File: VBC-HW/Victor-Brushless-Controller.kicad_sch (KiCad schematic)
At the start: 25 parts, among them Q1 TPH4R008NH, Q2 TPH4R008NH, Q3 TPH4R008NH, Q4 TPH4R008NH, Q5 TPH4R008NH, Q6 TPH4R008NH, U1 DRV8305NQPHPRQ1

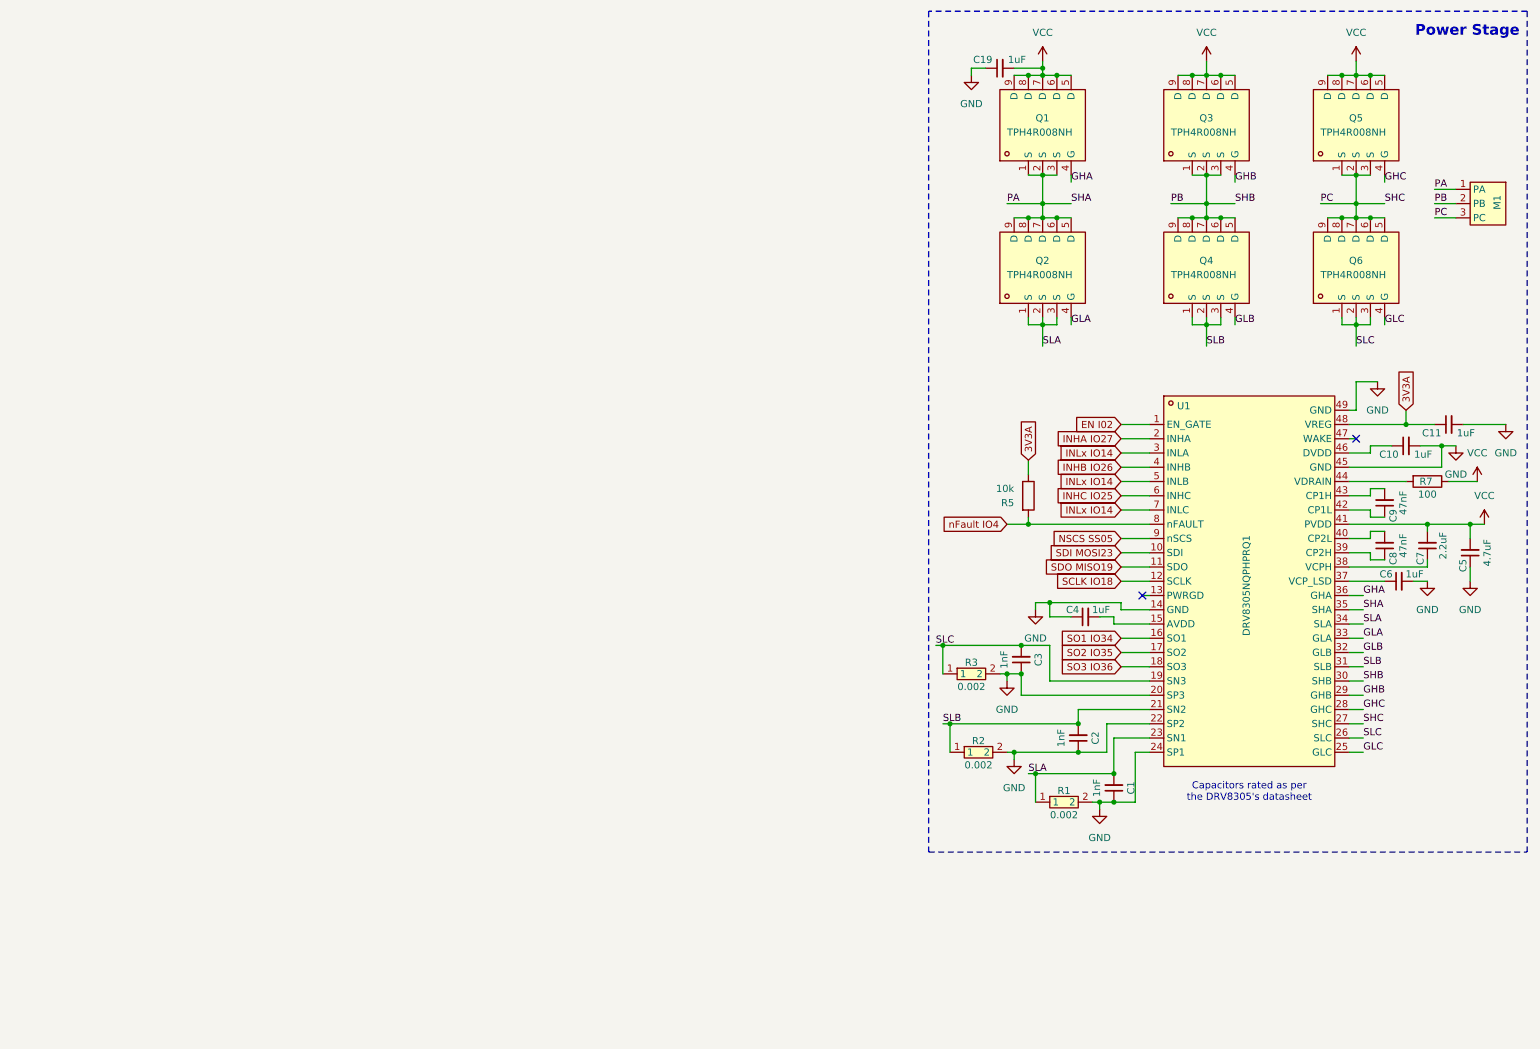
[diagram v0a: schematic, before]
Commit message: Added Kicad schematic magnetic, bus and temp
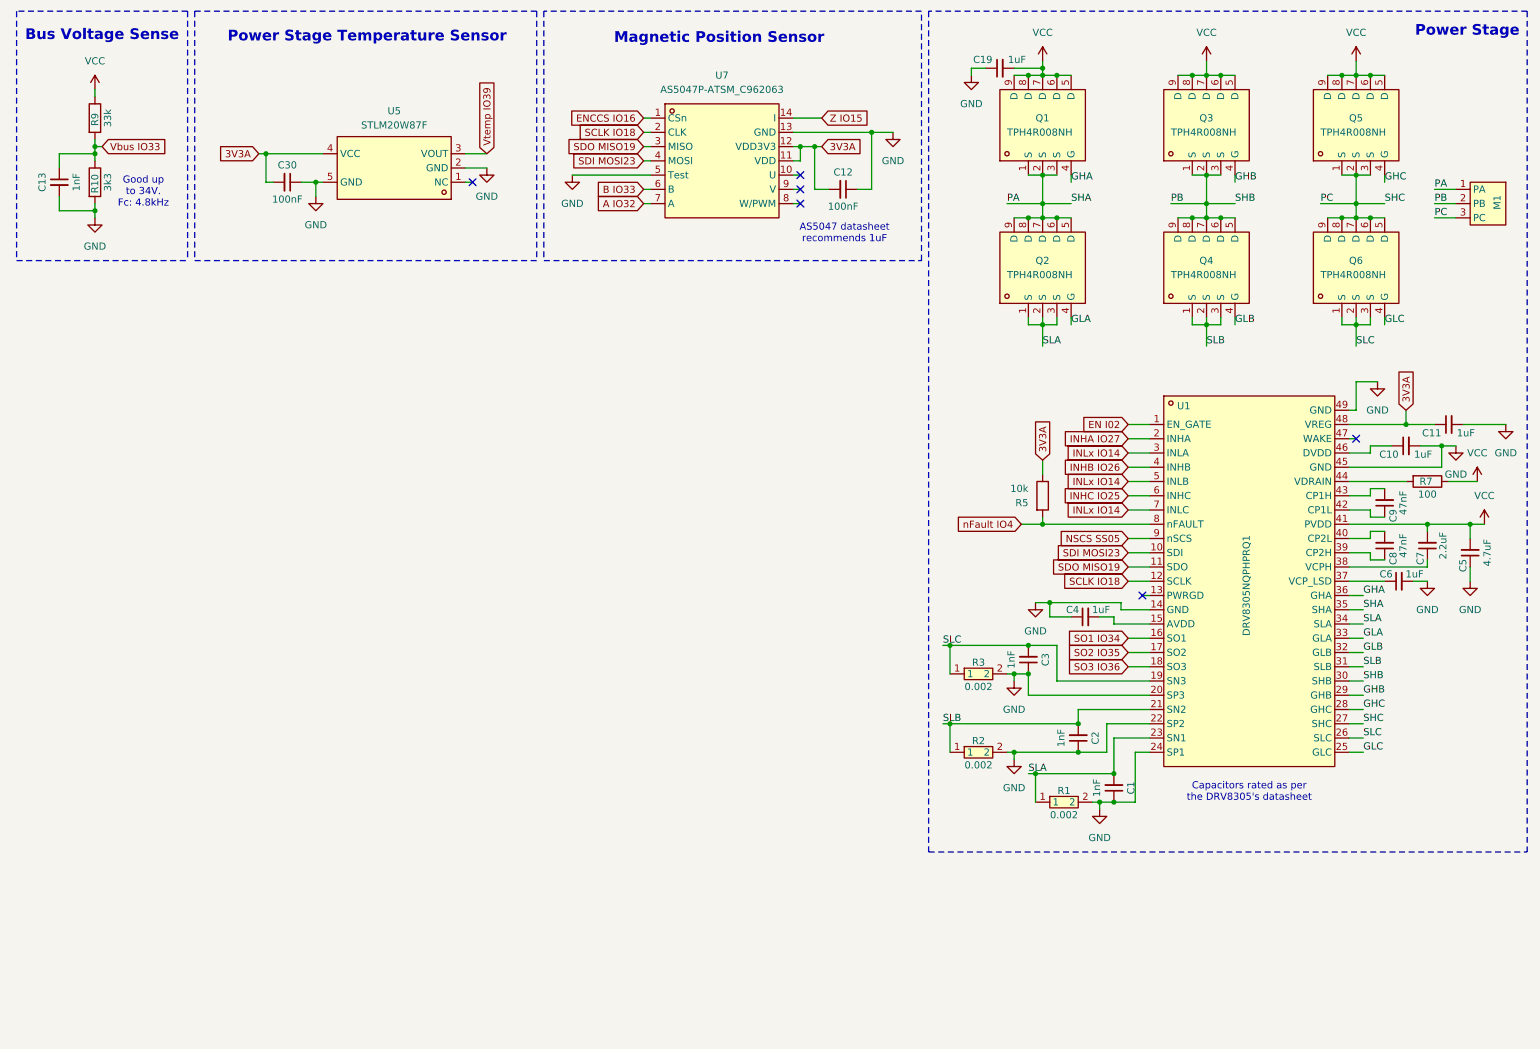
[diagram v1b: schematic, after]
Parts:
- added C12, C30: 100nF, symbol Device:C_Small
- added C13: 1nF, symbol Device:C_Small
- added R10: 3k3, symbol Device:R
- added R9: 33k, symbol Device:R
- added U5: STLM20W87F, easyeda2kicad:SOT-323-5_L2.1-W1.3-P0.65-LS2.1-BL, symbol STLM20W87F:STLM20W87F
- added U7: AS5047P-ATSM_C962063, easyeda2kicad:TSSOP-14_L5.0-W4.4-P0.65-LS6.4-BL, symbol AS5047P-ATSM:AS5047P-ATSM_C962063
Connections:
- net 3V3A: now also C12.2, C30.2, U5.4 (VCC), U7.11 (VDD), U7.12 (VDD3V3)
- net GND: now also C12.1, C13.2, C30.1, R10.2, U5.2 (GND), U5.5 (GND), U7.13 (GND), U7.5 (Test)
- net SCLK IO18: now also U7.2 (CLK)
- net SDI MOSI23: now also U7.4 (MOSI)
- net SDO MISO19: now also U7.3 (MISO)
- net VCC: now also R9.1
- new net A IO32: U7.7 (A)
- new net B IO33: U7.6 (B)
- new net ENCCS IO16: U7.1 (CSn)
- new net Vbus IO33: C13.1, R10.1, R9.2
- new net Vtemp IO39: U5.3 (VOUT)
- new net Z IO15: U7.14 (I)
- no-connect marks 2 -> 6
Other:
- note added: "AS5047 datasheet recommends 1uF"
- note added: "Bus Voltage Sense"
- note added: "Good up to 34V. Fc: 4.8kHz"
- note added: "Magnetic Position Sensor"
- note added: "Power Stage Temperature Sensor"
- moved on the sheet: C3, R3, R5

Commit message: Added buck converter
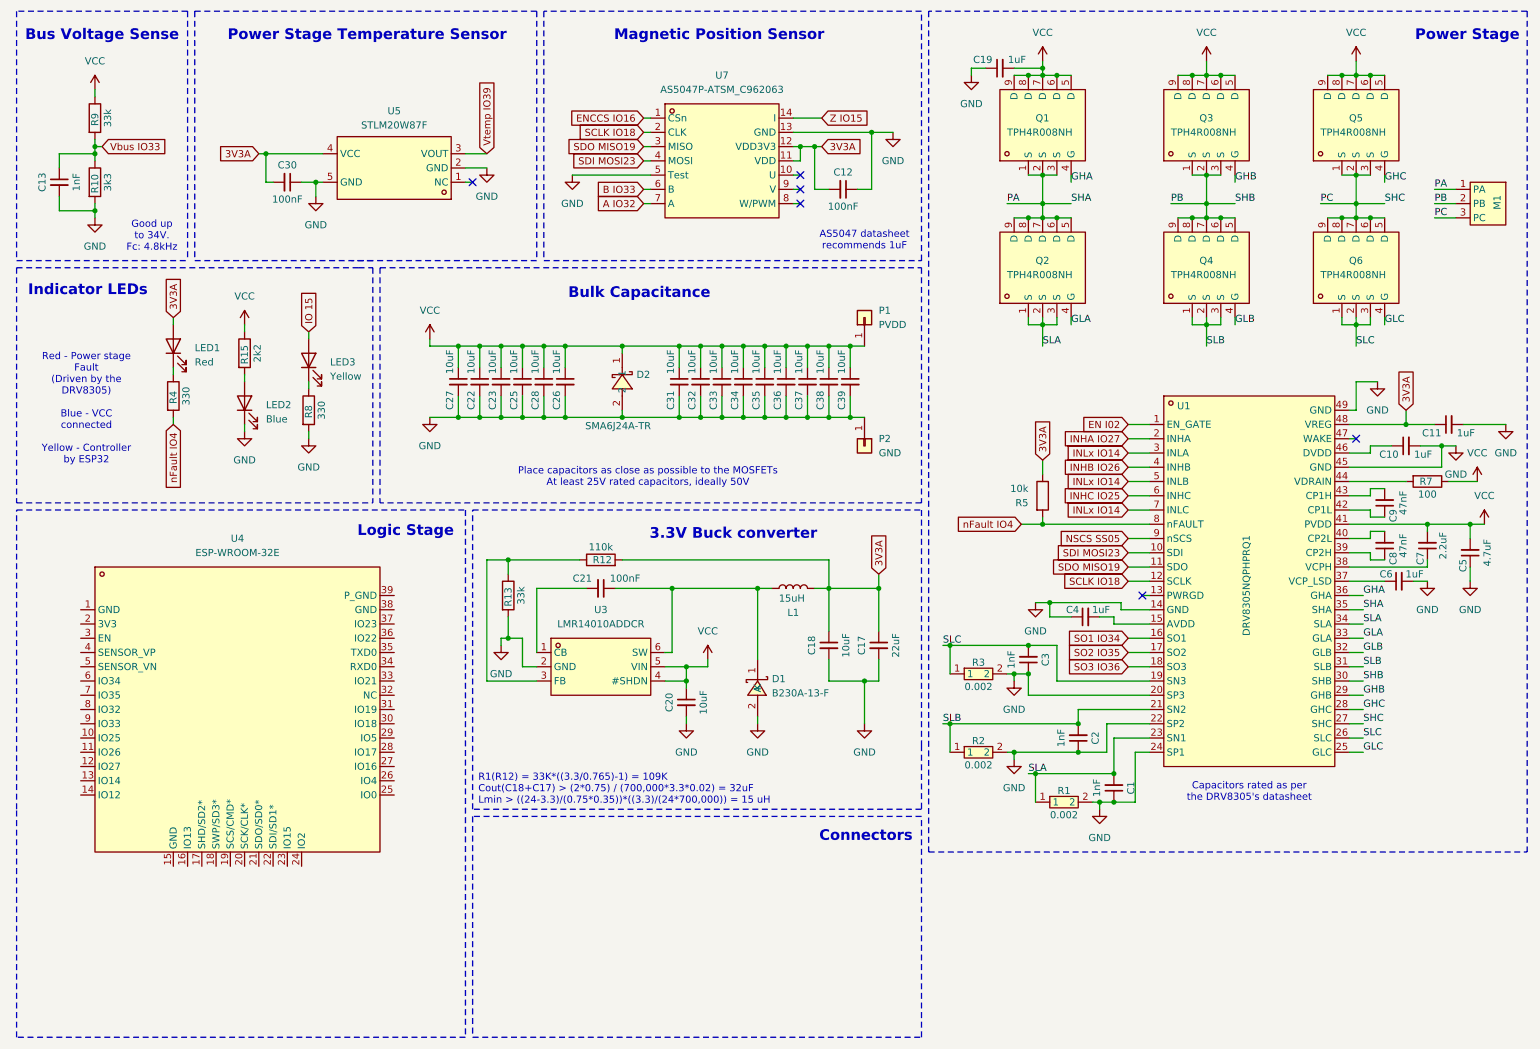
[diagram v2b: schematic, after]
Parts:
- added C17: 22uF, symbol Device:C_Small
- added C18, C20, C22, C23, C25, C26, C27, C28, C31, C32, C33, C34, C35, C36, C37, C38, C39: 10uF, symbol Device:C_Small
- added C21: 100nF, symbol Device:C_Small
- added D1: B230A-13-F, easyeda2kicad:SMA_L4.4-W2.6-LS5.0-RD, symbol B230A-13-F:B230A-13-F
- added D2: SMA6J24A-TR, easyeda2kicad:SMA_L4.3-W2.6-LS5.2-RD, symbol SMA6J24A:SMA6J24A-TR
- added L1: 15uH, symbol Device:L
- added LED1: Red, symbol Device:LED
- added LED2: Blue, symbol Device:LED
- added LED3: Yellow, symbol Device:LED
- added P1: PVDD, symbol Connector_Generic:Conn_01x01
- added P2: GND, symbol Connector_Generic:Conn_01x01
- added R12: 110k, symbol Device:R
- added R13: 33k, symbol Device:R
- added R15: 2k2, symbol Device:R
- added R4, R8: 330, symbol Device:R
- added U3: LMR14010ADDCR, easyeda2kicad:SOT-23-6_L2.9-W1.6-P0.95-LS2.8-BR, symbol LMR14010ADDCR:LMR14010ADDCR
- added U4: ESP-WROOM-32E, easyeda2kicad:COMM-SMD_ESP-WROOM-32D, symbol ESP-WROOM-32E:ESP-WROOM-32E
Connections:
- net 3V3A: now also C17.1, C18.1, L1.2, LED1.2 (A), R12.2
- net GND: now also C17.2, C18.2, C20.2, C22.2, C23.2, C25.2, C26.2, C27.2, C28.2, C31.2, C32.2, C33.2, C34.2, C35.2, C36.2, C37.2, C38.2, C39.2, D1.2 (A), D2.2, LED2.1 (K), P2.1 (Pin_1), R13.2, R8.2, U3.2 (GND)
- net VCC: now also C20.1, C22.1, C23.1, C25.1, C26.1, C27.1, C28.1, C31.1, C32.1, C33.1, C34.1, C35.1, C36.1, C37.1, C38.1, C39.1, D2.1, P1.1 (Pin_1), R15.1, U3.4 (#SHDN), U3.5 (VIN)
- net nFault IO4: now also R4.2
- new net: LED1.1 (K), R4.1
- new net: LED2.2 (A), R15.2
- new net: LED3.1 (K), R8.1
- new net: C21.1, D1.1 (K), L1.1, U3.6 (SW)
- new net: C21.2, U3.1 (CB)
- new net: R12.1, R13.1, U3.3 (FB)
- new net IO 15: LED3.2 (A)
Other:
- note added: "3.3V Buck converter"
- note added: "Bulk Capacitance"
- note added: "Connectors"
- note added: "Indicator LEDs"
- note added: "Logic Stage"
- note added: "Place capacitors as close as possible to the MOSFETs At least 25V rated capacitors, ideally 50V"
- note added: "R1(R12) = 33K*((3.3/0.765)-1) = 109K Cout(C18+C17) > (2*0.75) / (700,000*3.3*0.02) = 32uF Lmin > ((24-3.3)/(0.75*0.35))*((3.3)/(24*700,000)) = 15 uH"
- note added: "Red - Power stage Fault (Driven by the DRV8305) Blue - VCC connected Yellow - Controller by ESP32"
- company: (none) -> Victor Nan Fernandez-Ayala
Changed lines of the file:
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@@
 	(title_block
 		(title "Victor-Brushless-Controller")
+		(date "2025-05-27")
+		(rev "1.0")
+		(company "Victor Nan Fernandez-Ayala")
 	)

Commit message: Finished schematics connections
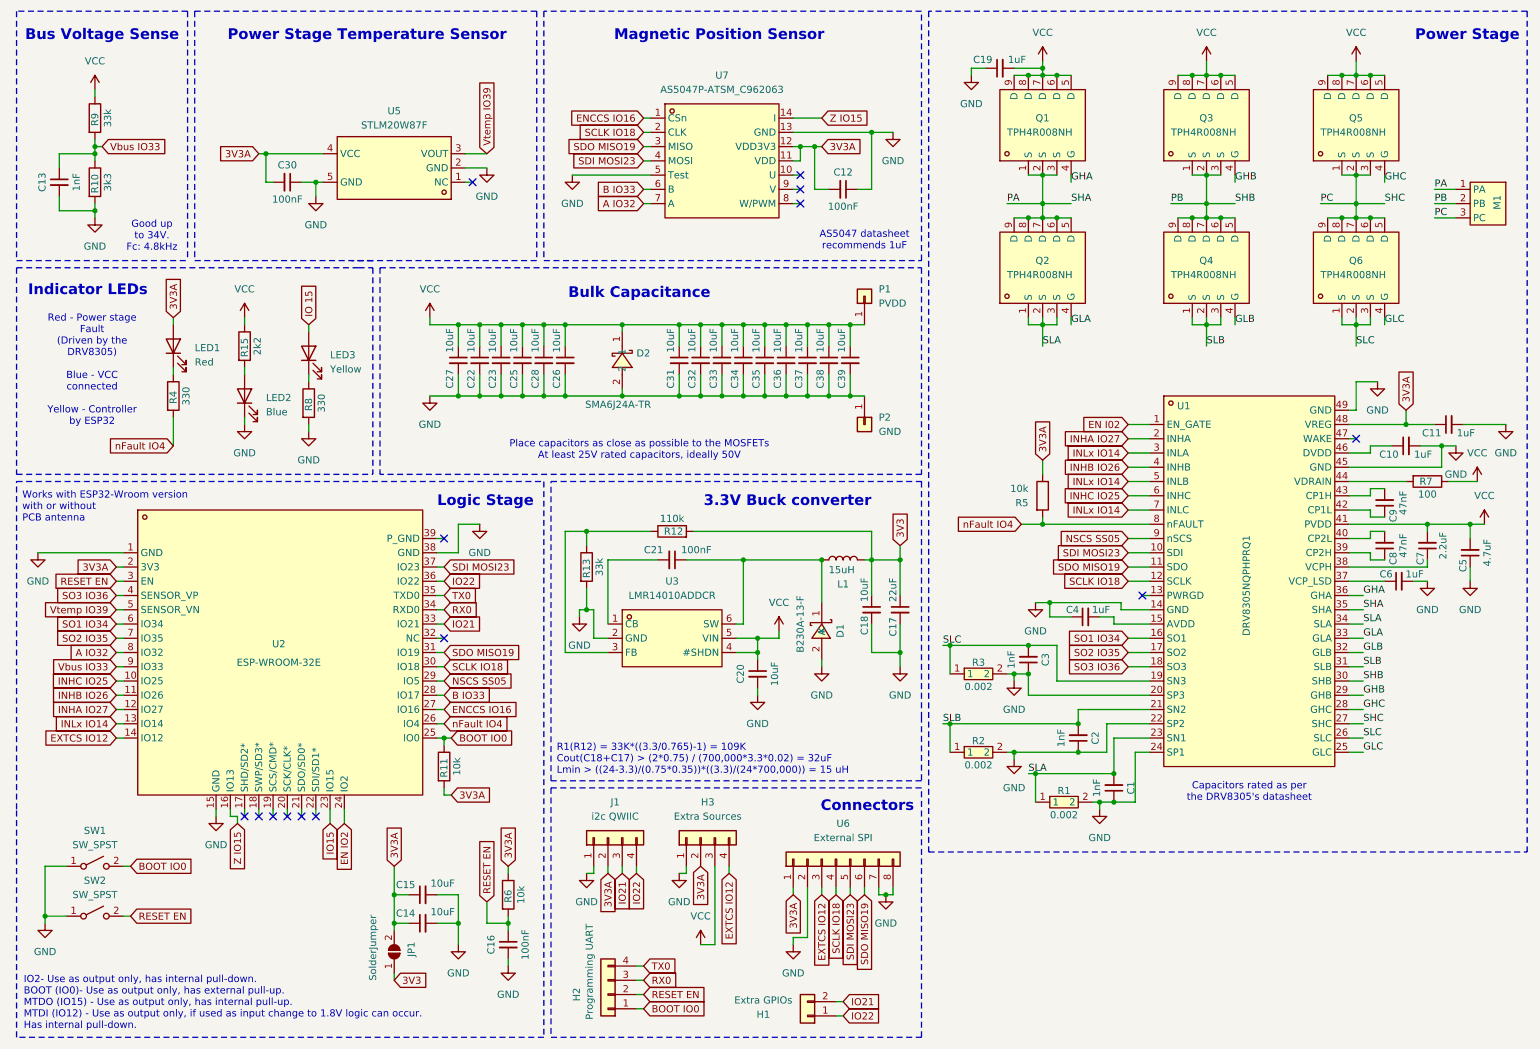
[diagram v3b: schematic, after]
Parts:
- removed U4: ESP-WROOM-32E, easyeda2kicad:COMM-SMD_ESP-WROOM-32D, symbol ESP-WROOM-32E:ESP-WROOM-32E
- added C14, C15: 10uF, symbol Device:C_Small
- added C16: 100nF, symbol Device:C_Small
- added H1: Extra GPIOs, symbol Connector_Generic:Conn_01x02
- added H2: Programming UART, symbol Connector_Generic:Conn_01x04
- added H3: Extra Sources, symbol Connector_Generic:Conn_01x04
- added J1: i2c QWIIC, symbol Connector_Generic:Conn_01x04
- added JP1: SolderJumper, symbol Jumper:SolderJumper_2_Open
- added R11, R6: 10k, symbol Device:R
- added SW1, SW2: SW_SPST, symbol Switch:SW_SPST
- added U2: ESP-WROOM-32E, easyeda2kicad:COMM-SMD_ESP-WROOM-32D, symbol ESP-WROOM-32E:ESP-WROOM-32E
- added U6: External SPI, symbol Connector_Generic:Conn_01x08
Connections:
- net 3V3A: now also C14.1, C15.1, H3.2 (Pin_2), J1.2 (Pin_2), JP1.2 (B), R11.2, R6.1, U2.2 (3V3), U6.1 (Pin_1); no longer C17.1, C18.1, L1.2, R12.2
- net A IO32: now also U2.8 (IO32)
- net B IO33: now also U2.28 (IO17)
- net ENCCS IO16: now also U2.27 (IO16)
- net GND: now also C14.2, C15.2, C16.2, H3.1 (Pin_1), J1.1 (Pin_1), SW1.1 (A), SW2.1 (A), U2.1 (GND), U2.15 (GND), U2.38 (GND), U6.2 (Pin_2), U6.7 (Pin_7), U6.8 (Pin_8)
- net INHA IO27: now also U2.12 (IO27)
- net INHB IO26: now also U2.11 (IO26)
- net INHC IO25: now also U2.10 (IO25)
- net INLx IO14: now also U2.13 (IO14)
- net NSCS SS05: now also U2.29 (IO5)
- net SCLK IO18: now also U2.30 (IO18), U6.4 (Pin_4)
- net SDI MOSI23: now also U2.37 (IO23), U6.5 (Pin_5)
- net SDO MISO19: now also U2.31 (IO19), U6.6 (Pin_6)
- net SO1 IO34: now also U2.6 (IO34)
- net SO2 IO35: now also U2.7 (IO35)
- net SO3 IO36: now also U2.4 (SENSOR_VP)
- net VCC: now also H3.3 (Pin_3)
- net Vbus IO33: now also U2.9 (IO33)
- net Vtemp IO39: now also U2.5 (SENSOR_VN)
- net Z IO15: now also U2.16 (IO13)
- net nFault IO4: now also U2.26 (IO4)
- new net 3V3: C17.1, C18.1, JP1.1 (A), L1.2, R12.2
- new net BOOT IO0: H2.1 (Pin_1), R11.1, SW1.2 (B), U2.25 (IO0)
- new net EN IO2: U2.24 (IO2)
- new net EXTCS IO12: H3.4 (Pin_4), U2.14 (IO12), U6.3 (Pin_3)
- new net IO15: U2.23 (IO15)
- new net IO21: H1.2 (Pin_2), J1.3 (Pin_3), U2.33 (IO21)
- new net IO22: H1.1 (Pin_1), J1.4 (Pin_4), U2.36 (IO22)
- new net RESET EN: C16.1, H2.2 (Pin_2), R6.2, SW2.2 (B), U2.3 (EN)
- new net RX0: H2.3 (Pin_3), U2.34 (RXD0)
- new net TX0: H2.4 (Pin_4), U2.35 (TXD0)
- no-connect marks 6 -> 14
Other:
- note added: "IO2- Use as output only, has internal pull-down. BOOT (IO0)- Use as output only, has external pull-up. MTDO (IO15) - Use as output only, has internal pull-up. MTDI (IO12) - Use as output only, if used as input change to 1.8V logic can occur. Has internal pull-down."
- note added: "Works with ESP32-Wroom version with or without PCB antenna"
- moved on the sheet: C17, C18, C20, C21, C22, C23, C25, C26, C27, C28, C31, C32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

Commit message: Started adding footprints
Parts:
- D1: footprint easyeda2kicad:SMA_L4.4-W2.6-LS5.0-RD -> B230A-13-F:B230A-13-F
- D2: footprint easyeda2kicad:SMA_L4.3-W2.6-LS5.2-RD -> SMA6J24A:SMA6J24A
- Q1, Q2, Q3, Q4, Q5, Q6: footprint easyeda2kicad:SOP-8_L5.0-W5.0-P1.27-LS6.0_TPH4R008NH-L1Q -> TPH4R008NH,L1Q(M:TPH4R008NH,L1Q(M
- U1: footprint easyeda2kicad:HTQFP-48_L7.0-W7.0-P0.50-LS9.0-BL-EP5.1 -> DRV8305NQPHPRQ1:DRV8305NQPHPRQ1
- U2: footprint easyeda2kicad:COMM-SMD_ESP-WROOM-32D -> ESP-WROOM-32E:ESP-WROOM-32E
- U3: footprint easyeda2kicad:SOT-23-6_L2.9-W1.6-P0.95-LS2.8-BR -> LMR14010ADDCR:LMR14010ADDCR
- U5: footprint easyeda2kicad:SOT-323-5_L2.1-W1.3-P0.65-LS2.1-BL -> STLM20W87F:STLM20W87F
- U7: footprint easyeda2kicad:TSSOP-14_L5.0-W4.4-P0.65-LS6.4-BL -> AS5047P-ATSM:AS5047P-ATSM

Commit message: Added footprints to schematic
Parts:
- C1, C13, C2, C3: footprint (none) -> 0402B102K500NT:0402B102K500NT
- C10, C11, C4, C6: footprint (none) -> CL05A105KA5NQNC:CL05A105KA5NQNC
- C12, C15, C16, C21, C30: footprint (none) -> CL05B104KO5NNNC:CL05B104KO5NNNC
- C14: footprint (none) -> CL05A106MQ5NUNC:CL05A106MQ5NUNC
- C17: footprint (none) -> CL10A226MQ8NRNC:CL10A226MQ8NRNC
- C18: footprint (none) -> CL10A106MA8NRNC:CL10A106MA8NRNC
- C19: footprint (none) -> CL10A105KB8NNNC:CL10A105KB8NNNC
- C20, C22, C23, C25, C26, C27, C31, C32, C33, C34, C35, C36, C39: footprint (none) -> GRM21BR61H106KE43L:GRM21BR61H106KE43L
- C24: renamed from C28; footprint (none) -> GRM21BR61H106KE43L:GRM21BR61H106KE43L
- C37, C38: footprint (none) -> 1206X106M500NT:1206X106M500NT
- C5: footprint (none) -> 1206B475K500NT:1206B475K500NT
- C7: footprint (none) -> CL31B225KBHNNNE:CL31B225KBHNNNE
- C8: footprint (none) -> CL21B473KCFNNNE:CL21B473KCFNNNE
- C9: footprint (none) -> CL10B473KB8NNNC:CL10B473KB8NNNC
- L1: footprint (none) -> PIS3D18P-150M-T:PIS3D18P-150M-T
- LED1: footprint (none) -> KT-0603R:KT-0603R
- LED2: footprint (none) -> 19-217:19-217
- LED3: footprint (none) -> 19-213:19-213
- R1, R2, R3: footprint easyeda2kicad:RES-SMD_L6.4-W3.2-R2512 -> CUM2512-24FR002:CUM2512-24FR002
- R10: footprint (none) -> 0402WGF3301TCE:0402WGF3301TCE
- R11, R5, R6: footprint (none) -> 0402WGF1002TCE:0402WGF1002TCE
- R12: footprint (none) -> RC0402FR-07110KL:RC0402FR-07110KL
- R13, R9: footprint (none) -> 0402WGF3302TCE:0402WGF3302TCE
- R15: footprint (none) -> 0402WGF2201TCE:0402WGF2201TCE
- R4, R8: footprint (none) -> 0402WGF3300TCE:0402WGF3300TCE
- R7: footprint (none) -> 0402WGF1000TCE:0402WGF1000TCE
- SW1, SW2: footprint (none) -> TS342A2P-WZ:TS342A2P-WZ
